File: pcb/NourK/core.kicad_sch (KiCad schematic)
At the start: 42 parts, among them IC2 IS31FL3733B-QFLS4-TR, J5 USB_C_Receptacle_USB2.0, J6 Conn_ARM_JTAG_SWD_10, SW28 SW_SPST_G, SW29 SW_SPST_G, U3 STM32L082CZYx, U4 AP2112K-3.3, Y3 8MHz, Y4 32.768KHz

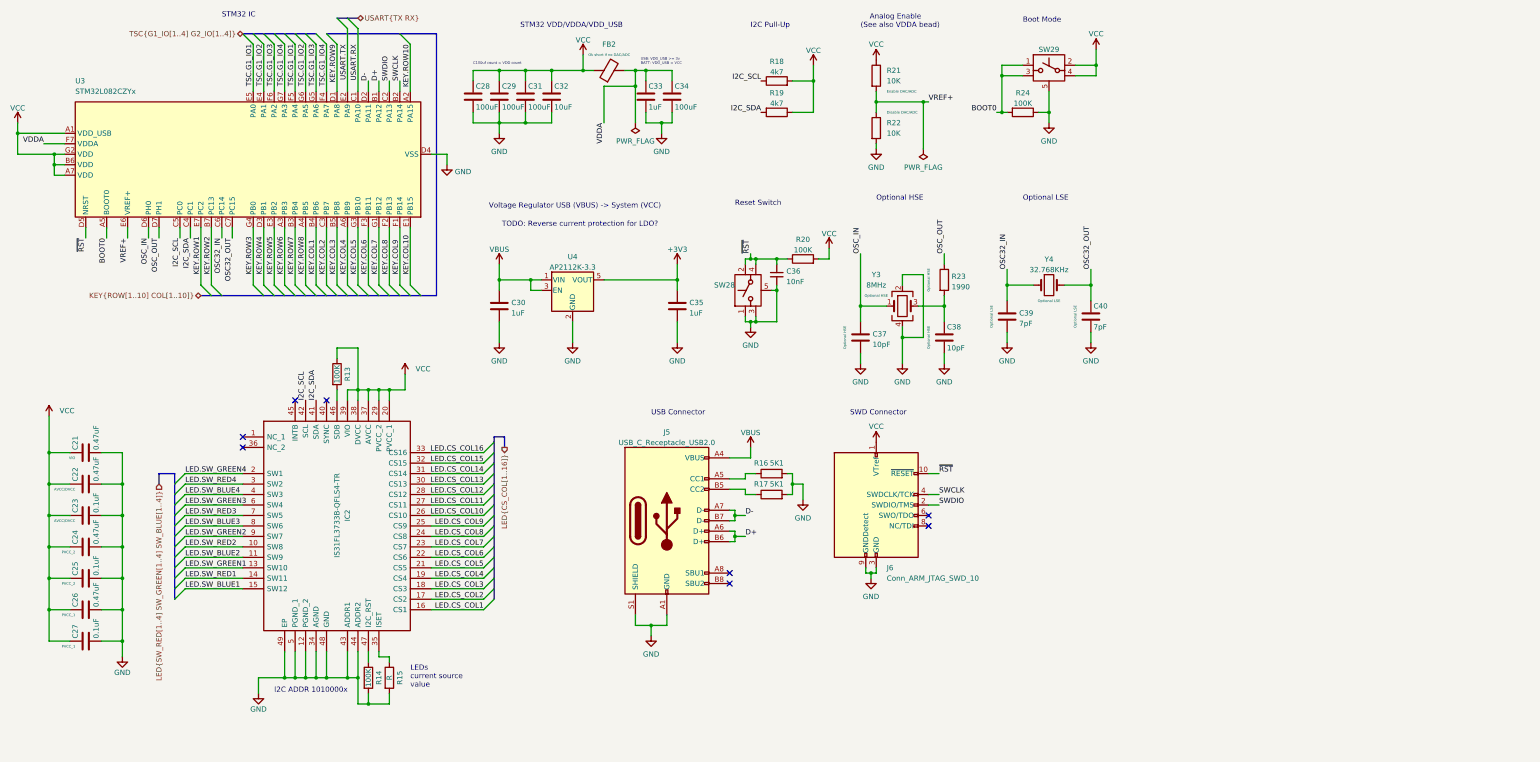
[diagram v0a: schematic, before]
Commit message: Re-traced RHS
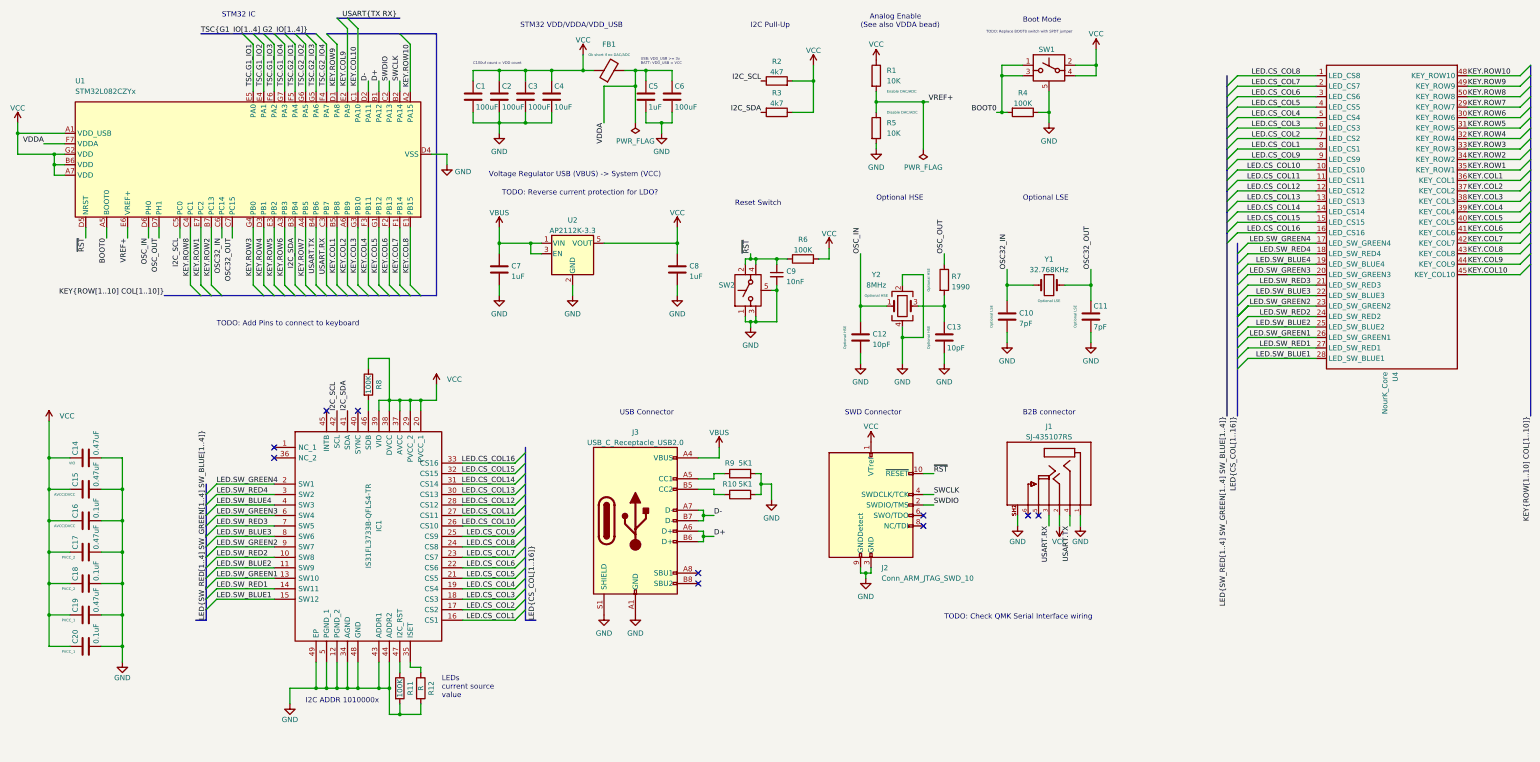
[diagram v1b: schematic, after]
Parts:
- added J1: SJ-435107RS, Nour_KB:CUI_SJ-435107RS, symbol Nour_KB:SJ-435107RS
- added U4: NourK_Core, Nour_KB:NourKB_Core, symbol Nour_KB:NourK_Core
- renumbered C28 to C1, C39 to C10, C40 to C11, C37 to C12, C38 to C13, C21 to C14, C22 to C15, C23 to C16, C24 to C17, C25 to C18, C26 to C19, C29 to C2, C27 to C20, C31 to C3, C32 to C4, C33 to C5, C34 to C6, C30 to C7, C35 to C8, C36 to C9, FB2 to FB1, IC2 to IC1, J6 to J2, J5 to J3, R21 to R1, R17 to R10, R14 to R11, R15 to R12, R18 to R2, R19 to R3, R24 to R4, R22 to R5, R20 to R6, R23 to R7, R13 to R8, R16 to R9, SW29 to SW1, SW28 to SW2, U3 to U1, U4 to U2, Y4 to Y1, Y3 to Y2
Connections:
- net +3V3 is gone; now on net VCC: C8.1, U2.5 (VOUT)
- net GND: now also J1.1, J1.SH1, J1.SH2
- net I2C_SDA: now also U1.B3 (PB4); no longer U1.C4 (PC1)
- net KEY.COL1: now also U1.B5 (PB8), U4.36 (KEY_COL1); no longer U1.B4 (PB6)
- net KEY.COL10: now also U1.C1 (PA10), U4.45 (KEY_COL10); no longer U1.E1 (PB15)
- net KEY.COL2: now also U1.A6 (PB9), U4.37 (KEY_COL2); no longer U1.C3 (PB7)
- net KEY.COL3: now also U1.G3 (PB10), U4.38 (KEY_COL3); no longer U1.B5 (PB8)
- net KEY.COL4: now also U1.F3 (PB11), U4.39 (KEY_COL4); no longer U1.A6 (PB9)
- net KEY.COL5: now also U1.G1 (PB12), U4.40 (KEY_COL5); no longer U1.G3 (PB10)
- net KEY.COL6: now also U1.F2 (PB13), U4.41 (KEY_COL6); no longer U1.F3 (PB11)
- net KEY.COL7: now also U1.F1 (PB14), U4.42 (KEY_COL7); no longer U1.G1 (PB12)
- net KEY.COL8: now also U1.E1 (PB15), U4.43 (KEY_COL8); no longer U1.F2 (PB13)
- net KEY.COL9: now also U1.E2 (PA9), U4.44 (KEY_COL9); no longer U1.F1 (PB14)
- net KEY.ROW1: now also U4.35 (KEY_ROW1)
- net KEY.ROW10: now also U4.48 (KEY_ROW10)
- net KEY.ROW2: now also U4.34 (KEY_ROW2)
- net KEY.ROW3: now also U4.33 (KEY_ROW3)
- net KEY.ROW4: now also U4.32 (KEY_ROW4)
- net KEY.ROW5: now also U4.31 (KEY_ROW5)
- net KEY.ROW6: now also U4.30 (KEY_ROW6)
- net KEY.ROW7: now also U1.A4 (PB5), U4.29 (KEY_ROW7); no longer U1.B3 (PB4)
- net KEY.ROW8: now also U1.C4 (PC1), U4.50 (KEY_ROW8); no longer U1.A4 (PB5)
- net KEY.ROW9: now also U4.49 (KEY_ROW9)
- net LED.CS_COL1: now also U4.8 (LED_CS1)
- net LED.CS_COL10: now also U4.10 (LED_CS10)
- net LED.CS_COL11: now also U4.11 (LED_CS11)
- net LED.CS_COL12: now also U4.12 (LED_CS12)
- net LED.CS_COL13: now also U4.13 (LED_CS13)
- net LED.CS_COL14: now also U4.14 (LED_CS14)
- net LED.CS_COL15: now also U4.15 (LED_CS15)
- net LED.CS_COL16: now also U4.16 (LED_CS16)
- net LED.CS_COL2: now also U4.7 (LED_CS2)
- net LED.CS_COL3: now also U4.6 (LED_CS3)
- net LED.CS_COL4: now also U4.5 (LED_CS4)
- net LED.CS_COL5: now also U4.4 (LED_CS5)
- net LED.CS_COL6: now also U4.3 (LED_CS6)
- net LED.CS_COL7: now also U4.2 (LED_CS7)
- net LED.CS_COL8: now also U4.1 (LED_CS8)
- net LED.CS_COL9: now also U4.9 (LED_CS9)
- net LED.SW_BLUE1: now also U4.28 (LED_SW_BLUE1)
- net LED.SW_BLUE2: now also U4.25 (LED_SW_BLUE2)
- net LED.SW_BLUE3: now also U4.22 (LED_SW_BLUE3)
- net LED.SW_BLUE4: now also U4.19 (LED_SW_BLUE4)
- net LED.SW_GREEN1: now also U4.26 (LED_SW_GREEN1)
- net LED.SW_GREEN2: now also U4.23 (LED_SW_GREEN2)
- net LED.SW_GREEN3: now also U4.20 (LED_SW_GREEN3)
- net LED.SW_GREEN4: now also U4.17 (LED_SW_GREEN4)
- net LED.SW_RED1: now also U4.27 (LED_SW_RED1)
- net LED.SW_RED2: now also U4.24 (LED_SW_RED2)
- net LED.SW_RED3: now also U4.21 (LED_SW_RED3)
- net LED.SW_RED4: now also U4.18 (LED_SW_RED4)
- net TSC.G1_IO1: no longer U1.F5 (PA4)
- net TSC.G1_IO2: no longer U1.G6 (PA5)
- net TSC.G1_IO3: no longer U1.G5 (PA6)
- net TSC.G1_IO4: no longer U1.F4 (PA7)
- net USART.RX: now also U1.C3 (PB7), J1.3; no longer U1.C1 (PA10)
- net USART.TX: now also U1.B4 (PB6), J1.4; no longer U1.E2 (PA9)
- net VCC: now also J1.2
- new net TSC.G2_IO1: U1.F5 (PA4)
- new net TSC.G2_IO2: U1.G6 (PA5)
- new net TSC.G2_IO3: U1.G5 (PA6)
- new net TSC.G2_IO4: U1.F4 (PA7)
- no-connect marks 8 -> 10
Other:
- note added: "B2B connector"
- note added: "TODO: Add Pins to connect to keyboard"
- note added: "TODO: Check QMK Serial Interface wiring"
- note added: "TODO: Replace BOOT0 switch with SPDT jumper"
- moved on the sheet: C14, C15, C16, C17, C18, C19, C20, C7, C8, IC1, J2, J3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

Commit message: Initial RHS DRC checked
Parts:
- U1: footprint Package_CSP:ST_WLCSP-49_Die447 -> Nour_KB:ST_WLCSP-49_Die447
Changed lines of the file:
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@@
       (effects (font (size 1.27 1.27)) (justify right))
     )
-    (property "Footprint" "Package_CSP:ST_WLCSP-49_Die447" (id 2) (at 114.3 66.04 0)
+    (property "Footprint" "Nour_KB:ST_WLCSP-49_Die447" (id 2) (at 114.3 66.04 0)
       (effects (font (size 1.27 1.27)) (justify right) hide)
     )

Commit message: RHS and LHS wire complete and initial DRC
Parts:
- U4: footprint Nour_KB:NourKB_Core -> Nour_KB:NourKB_Core_2
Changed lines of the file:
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@@
       (effects (font (size 1.27 1.27)) (justify left))
     )
-    (property "Footprint" "Nour_KB:NourKB_Core" (id 2) (at 352.425 64.77 0)
+    (property "Footprint" "Nour_KB:NourKB_Core_2" (id 2) (at 352.425 64.77 0)
       (effects (font (size 1.27 1.27)) hide)
     )

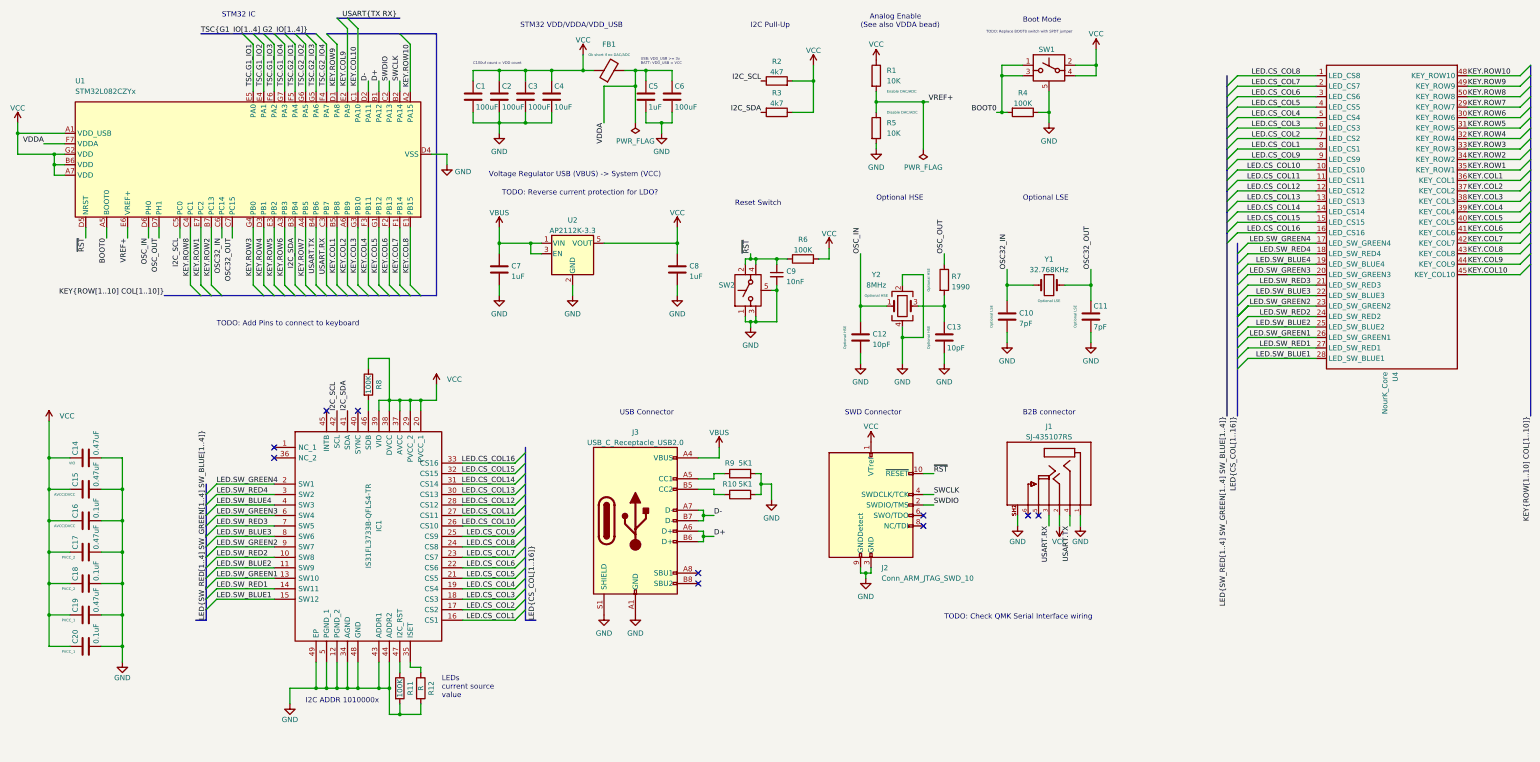
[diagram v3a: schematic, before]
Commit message: Update schematics to match new footprints
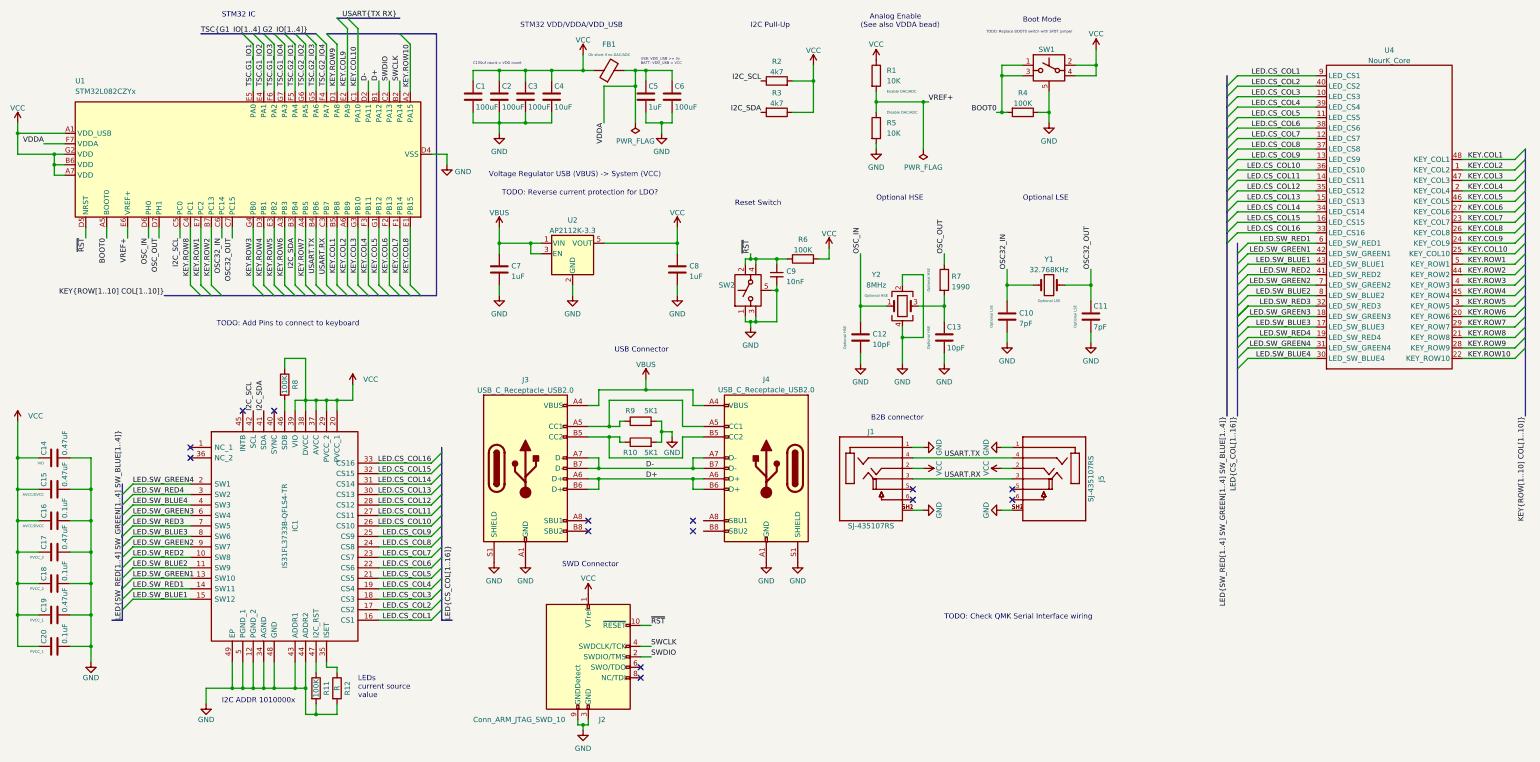
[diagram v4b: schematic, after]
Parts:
- added J4: USB_C_Receptacle_USB2.0, Nour_KB:GCT_USB4085-GF-A_REVA4, symbol Connector:USB_C_Receptacle_USB2.0
- added J5: SJ-435107RS, Nour_KB:CUI_SJ-435107RS, symbol Nour_KB:SJ-435107RS
- U4: symbol Nour_KB:NourK_Core -> Nour_KB:NourK_Core_3
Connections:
- net D+: now also J4.A6 (D+), J4.B6 (D+)
- net D-: now also J4.A7 (D-), J4.B7 (D-)
- net GND: now also J4.A1 (GND), J4.A12 (GND), J4.B1 (GND), J4.B12 (GND), J4.S1 (SHIELD), J5.1, J5.SH1, J5.SH2
- net KEY.COL1: now also U4.48 (KEY_COL1); no longer U4.36 (KEY_COL1)
- net KEY.COL10: now also U4.25 (KEY_COL10); no longer U4.45 (KEY_COL10)
- net KEY.COL2: now also U4.1 (KEY_COL2); no longer U4.37 (KEY_COL2)
- net KEY.COL3: now also U4.47 (KEY_COL3); no longer U4.38 (KEY_COL3)
- net KEY.COL4: now also U4.2 (KEY_COL4); no longer U4.39 (KEY_COL4)
- net KEY.COL5: now also U4.46 (KEY_COL5); no longer U4.40 (KEY_COL5)
- net KEY.COL6: now also U4.27 (KEY_COL6); no longer U4.41 (KEY_COL6)
- net KEY.COL7: now also U4.23 (KEY_COL7); no longer U4.42 (KEY_COL7)
- net KEY.COL8: now also U4.26 (KEY_COL8); no longer U4.43 (KEY_COL8)
- net KEY.COL9: now also U4.24 (KEY_COL9); no longer U4.44 (KEY_COL9)
- net KEY.ROW1: now also U4.5 (KEY_ROW1); no longer U4.35 (KEY_ROW1)
- net KEY.ROW10: now also U4.22 (KEY_ROW10); no longer U4.48 (KEY_ROW10)
- net KEY.ROW2: now also U4.44 (KEY_ROW2); no longer U4.34 (KEY_ROW2)
- net KEY.ROW3: now also U4.4 (KEY_ROW3); no longer U4.33 (KEY_ROW3)
- net KEY.ROW4: now also U4.45 (KEY_ROW4); no longer U4.32 (KEY_ROW4)
- net KEY.ROW5: now also U4.3 (KEY_ROW5); no longer U4.31 (KEY_ROW5)
- net KEY.ROW6: now also U4.20 (KEY_ROW6); no longer U4.30 (KEY_ROW6)
- net KEY.ROW8: now also U4.21 (KEY_ROW8); no longer U4.50 (KEY_ROW8)
- net KEY.ROW9: now also U4.28 (KEY_ROW9); no longer U4.49 (KEY_ROW9)
- net LED.CS_COL1: now also U4.9 (LED_CS1); no longer U4.8 (LED_CS1)
- net LED.CS_COL10: now also U4.36 (LED_CS10); no longer U4.10 (LED_CS10)
- net LED.CS_COL11: now also U4.14 (LED_CS11); no longer U4.11 (LED_CS11)
- net LED.CS_COL12: now also U4.35 (LED_CS12); no longer U4.12 (LED_CS12)
- net LED.CS_COL13: now also U4.15 (LED_CS13); no longer U4.13 (LED_CS13)
- net LED.CS_COL14: now also U4.34 (LED_CS14); no longer U4.14 (LED_CS14)
- net LED.CS_COL15: now also U4.16 (LED_CS15); no longer U4.15 (LED_CS15)
- net LED.CS_COL16: now also U4.33 (LED_CS16); no longer U4.16 (LED_CS16)
- net LED.CS_COL2: now also U4.40 (LED_CS2); no longer U4.7 (LED_CS2)
- net LED.CS_COL3: now also U4.10 (LED_CS3); no longer U4.6 (LED_CS3)
- net LED.CS_COL4: now also U4.39 (LED_CS4); no longer U4.5 (LED_CS4)
- net LED.CS_COL5: now also U4.11 (LED_CS5); no longer U4.4 (LED_CS5)
- net LED.CS_COL6: now also U4.38 (LED_CS6); no longer U4.3 (LED_CS6)
- net LED.CS_COL7: now also U4.12 (LED_CS7); no longer U4.2 (LED_CS7)
- net LED.CS_COL8: now also U4.37 (LED_CS8); no longer U4.1 (LED_CS8)
- net LED.CS_COL9: now also U4.13 (LED_CS9); no longer U4.9 (LED_CS9)
- net LED.SW_BLUE1: now also U4.43 (LED_SW_BLUE1); no longer U4.28 (LED_SW_BLUE1)
- net LED.SW_BLUE2: now also U4.8 (LED_SW_BLUE2); no longer U4.25 (LED_SW_BLUE2)
- net LED.SW_BLUE3: now also U4.17 (LED_SW_BLUE3); no longer U4.22 (LED_SW_BLUE3)
- net LED.SW_BLUE4: now also U4.30 (LED_SW_BLUE4); no longer U4.19 (LED_SW_BLUE4)
- net LED.SW_GREEN1: now also U4.42 (LED_SW_GREEN1); no longer U4.26 (LED_SW_GREEN1)
- net LED.SW_GREEN2: now also U4.7 (LED_SW_GREEN2); no longer U4.23 (LED_SW_GREEN2)
- net LED.SW_GREEN3: now also U4.18 (LED_SW_GREEN3); no longer U4.20 (LED_SW_GREEN3)
- net LED.SW_GREEN4: now also U4.31 (LED_SW_GREEN4); no longer U4.17 (LED_SW_GREEN4)
- net LED.SW_RED1: now also U4.6 (LED_SW_RED1); no longer U4.27 (LED_SW_RED1)
- net LED.SW_RED2: now also U4.41 (LED_SW_RED2); no longer U4.24 (LED_SW_RED2)
- net LED.SW_RED3: now also U4.32 (LED_SW_RED3); no longer U4.21 (LED_SW_RED3)
- net LED.SW_RED4: now also U4.19 (LED_SW_RED4); no longer U4.18 (LED_SW_RED4)
- net USART.RX: now also J5.3
- net USART.TX: now also J5.4
- net VBUS: now also J4.A4 (VBUS), J4.A9 (VBUS), J4.B4 (VBUS), J4.B9 (VBUS)
- net VCC: now also J5.2
- net at J3.A5 (CC1), R9.1: now also J4.A5 (CC1)
- net at J3.B5 (CC2), R10.1: now also J4.B5 (CC2)
- no-connect marks 10 -> 14
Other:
- moved on the sheet: C14, C15, C16, C17, C18, C19, C20, IC1, J1, J2, J3, R10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

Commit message: Draft wire the core
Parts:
- removed SW1: SW_SPST_G, Nour_KB:EVQP9102W, symbol Nour_KB:SW_Push_SPST_13_24_G
- added C21: 100nF, Capacitor_SMD:C_0805_2012Metric, symbol Device:C
- added R13, R14: 5K1, Resistor_SMD:R_0805_2012Metric, symbol Device:R
- added SW1: SW_SPDT, Nour_KB:CSS-1211TB, symbol Switch:SW_SPDT
- C1, C2, C3, C6: value 100uF -> 100nF
- R4: value 100K -> 10K
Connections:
- net BOOT0: now also R4.1; no longer R4.2
- net GND: now also C21.2, R13.1, R14.1, SW1.1 (A); no longer R4.1
- net KEY.COL1: now also U1.G3 (PB10); no longer U1.B5 (PB8)
- net KEY.COL10: now also U1.F1 (PB14); no longer U1.C1 (PA10)
- net KEY.COL2: now also U1.F2 (PB13); no longer U1.A6 (PB9)
- net KEY.COL3: now also U1.G4 (PB0); no longer U1.G3 (PB10)
- net KEY.COL5: now also U1.B7 (PC13); no longer U1.G1 (PB12)
- net KEY.COL6: now also U1.D1 (PA8); no longer U1.F2 (PB13)
- net KEY.COL7: now also U1.E3 (PB2); no longer U1.F1 (PB14)
- net KEY.COL9: now also U1.G1 (PB12); no longer U1.E2 (PA9)
- net KEY.ROW1: now also U1.C4 (PC1); no longer U1.E7 (PC2)
- net KEY.ROW10: now also U1.E2 (PA9); no longer U1.A2 (PA15)
- net KEY.ROW2: now also U1.A4 (PB5); no longer U1.B7 (PC13)
- net KEY.ROW3: now also U1.A6 (PB9); no longer U1.G4 (PB0)
- net KEY.ROW4: now also U1.B5 (PB8); no longer U1.D3 (PB1)
- net KEY.ROW5: now also U1.E7 (PC2); no longer U1.E3 (PB2)
- net KEY.ROW6: now also U1.A2 (PA15); no longer U1.A3 (PB3)
- net KEY.ROW7: now also U1.A3 (PB3); no longer U1.A4 (PB5)
- net KEY.ROW8: now also U1.C1 (PA10); no longer U1.C4 (PC1)
- net KEY.ROW9: now also U1.D3 (PB1); no longer U1.D1 (PA8)
- net LED.SW_BLUE1: now also IC1.11 (SW9); no longer IC1.15 (SW12)
- net LED.SW_BLUE2: now also IC1.15 (SW12); no longer IC1.11 (SW9)
- net LED.SW_BLUE3: now also IC1.4 (SW3); no longer IC1.8 (SW6)
- net LED.SW_BLUE4: now also IC1.8 (SW6); no longer IC1.4 (SW3)
- net LED.SW_GREEN1: now also IC1.9 (SW7); no longer IC1.13 (SW10)
- net LED.SW_GREEN2: now also IC1.13 (SW10); no longer IC1.9 (SW7)
- net LED.SW_GREEN3: now also IC1.2 (SW1); no longer IC1.6 (SW4)
- net LED.SW_GREEN4: now also IC1.6 (SW4); no longer IC1.2 (SW1)
- net LED.SW_RED1: now also IC1.10 (SW8); no longer IC1.14 (SW11)
- net LED.SW_RED2: now also IC1.14 (SW11); no longer IC1.10 (SW8)
- net LED.SW_RED3: now also IC1.3 (SW2); no longer IC1.7 (SW5)
- net LED.SW_RED4: now also IC1.7 (SW5); no longer IC1.3 (SW2)
- net USART.RX: now also J5.4; no longer J5.3
- net USART.TX: now also J5.3; no longer J5.4
- net VCC: now also C21.1, SW1.3 (C)
- net at J3.A5 (CC1), R9.1: no longer J4.A5 (CC1)
- net at J3.B5 (CC2), R10.1: no longer J4.B5 (CC2)
- new net: R4.2, SW1.2 (B)
- new net: J4.A5 (CC1), R13.2
- new net: J4.B5 (CC2), R14.2
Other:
- note added: "C100nf count = VDD count + VDD_USB"
- note added: "TODO: Switch power off when unplugging the jack"
- note removed: "C100uf count = VDD count"
- note removed: "TODO: Replace BOOT0 switch with SPDT jumper"
- moved on the sheet: C1, C2, C3, C4, R10, R4, R9
